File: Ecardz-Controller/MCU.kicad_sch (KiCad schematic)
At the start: 27 parts, among them J2 Conn_01x05, J5 Conn_01x04, U2 STM32G0C1RETx

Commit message: added eink and lcd pinouts
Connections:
- net LCD_PWM_BRIGHT: now reaches U2.28 (PB1)
- net SPI_LCD_DC: now reaches U2.29 (PB2)
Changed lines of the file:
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@@
+	(wire
+		(pts
+			(xy 137.16 93.98) (xy 161.29 93.98)
+		)
+		(stroke
+			(width 0)
+			(type default)
+		)
+	)
 	(wire
 		(pts
@@
 		(pts
 			(xy 85.09 50.8) (xy 69.85 50.8)
+		)
+		(stroke
+			(width 0)
+			(type default)
+		)
+	)
+	(wire
+		(pts
+			(xy 137.16 91.44) (xy 161.29 91.44)
 		)
 		(stroke
@@
 		)
 	)
+	(hierarchical_label "SPI_LCD_DC"
+		(shape input)
+		(at 161.29 93.98 0)
+		(fields_autoplaced yes)
+		(effects
+			(font
+				(size 1.27 1.27)
+			)
+			(justify left)
+		)
+	)
 	(hierarchical_label "USBC_UART_TX"
 		(shape input)
@@
 		(fields_autoplaced yes)
 		(effects
+			(font
+				(size 1.27 1.27)
+			)
+			(justify left)
+		)
+	)
+	(hierarchical_label "LCD_PWM_BRIGHT"
+		(shape input)
+		(at 161.29 91.44 0)
+		(fields_autoplaced yes)
+		(effects

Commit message: finished buzzer and button connections
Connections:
- net BUTTON6: now also U2.41 (PD9); no longer U2.37 (PA9/UCPD1_DBCC1)
- net BUZZER: now also U2.37 (PA9/UCPD1_DBCC1); no longer U2.41 (PD9)
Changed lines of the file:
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@@
-		)
-	)
-	(label "BUTTON6"
-		(at 139.7 68.58 0)
-		(fields_autoplaced yes)
-		(effects
-			(font
-				(size 1.27 1.27)
-			)
-			(justify left bottom)
 		)
 	)
@@
 		)
 	)
+	(label "BUTTON6"
+		(at 77.47 81.28 0)
+		(fields_autoplaced yes)
+		(effects
+			(font
+				(size 1.27 1.27)
+			)
+			(justify left bottom)
+		)
+	)
 	(label "SD_MISO"
 		(at 80.01 114.3 0)
@@
 		)
 	)
+	(hierarchical_label "BUTTONS"
+		(shape input)
+		(at 48.26 43.18 180)
+		(fields_autoplaced yes)
+		(effects
+			(font
+				(size 1.27 1.27)
+			)
+			(justify right)
+		)
+	)
+	(hierarchical_label "I2C_NFC_SCL"
+		(shape input)
+		(at 196.85 99.06 0)
+		(fields_autoplaced yes)
+		(effects
+			(font
+				(size 1.27 1.27)
+			)
+			(justify left)
+		)
+	)
+	(hierarchical_label "SPI_LCD_CS"
+		(shape input)
+		(at 161.29 88.9 0)
+		(fields_autoplaced yes)
+		(effects
+			(font
+				(size 1.27 1.27)
+			)
+			(justify left)
+		)
+	)
+	(hierarchical_label "SPI_EINK_SDA"
+		(shape input)
+		(at 74.93 88.9 180)
+		(fields_autoplaced yes)
+		(effects
+			(font
+				(size 1.27 1.27)
+			)
+			(justify right)
+		)
+	)
+	(hierarchical_label "SPI_EINK_CS"
+		(shape input)
+		(at 74.93 91.44 180)
+		(fields_autoplaced yes)
+		(effects
+			(font
+				(size 1.27 1.27)
+			)
+			(justify right)
+		)
+	)
+	(hierarchical_label "NFC_BUSY"
+		(shape input)
+		(at 196.85 101.6 0)
+		(fields_autoplaced yes)
+		(effects
+			(font
+				(size 1.27 1.27)
+			)
+			(justify left)
+		)
+	)
+	(hierarchical_label "SPI_LCD_MISO"
+		(shape input)
+		(at 161.29 60.96 0)
+		(fields_autoplaced yes)
+		(effects
+			(font
+				(size 1.27 1.27)
+			)
+			(justify left)
+		)
+	)
+	(hierarchical_label "NFC_I_SENSE"
+		(shape input)
+		(at 161.29 50.8 0)
+		(fields_autoplaced yes)
+		(effects
+			(font
+				(size 1.27 1.27)
+			)
+			(justify left)
+		)
+	)
+	(hierarchical_label "SPI_LCD_DC"
+		(shape input)
+		(at 161.29 93.98 0)
+		(fields_autoplaced yes)
+		(effects
+			(font
+				(size 1.27 1.27)
+			)
+			(justify left)
+		)
+	)
 	(hierarchical_label "BUZZER"
 		(shape input)
-		(at 74.93 81.28 180)
-		(fields_autoplaced yes)
-		(effects
-			(font
-				(size 1.27 1.27)
-			)
-			(justify right)
-		)
-	)
-	(hierarchical_label "BUTTONS"
-		(shape input)
-		(at 48.26 43.18 180)
-		(fields_autoplaced yes)
-		(effects
-			(font
-				(size 1.27 1.27)
-			)
-			(justify right)
-		)
-	)
-	(hierarchical_label "I2C_NFC_SCL"
-		(shape input)
-		(at 196.85 99.06 0)
-		(fields_autoplaced yes)
-		(effects
-			(font
-				(size 1.27 1.27)
-			)
-			(justify left)
-		)
-	)
-	(hierarchical_label "SPI_LCD_CS"
-		(shape input)
-		(at 161.29 88.9 0)
-		(fields_autoplaced yes)
-		(effects
-			(font
-				(size 1.27 1.27)
-			)
-			(justify left)
-		)
-	)
-	(hierarchical_label "SPI_EINK_SDA"
-		(shape input)
-		(at 74.93 88.9 180)
-		(fields_autoplaced yes)
-		(effects
-			(font
-				(size 1.27 1.27)
-			)
-			(justify right)
-		)
-	)
-	(hierarchical_label "SPI_EINK_CS"
-		(shape input)
-		(at 74.93 91.44 180)
-		(fields_autoplaced yes)
-		(effects
-			(font
-				(size 1.27 1.27)
-			)
-			(justify right)
-		)
-	)
-	(hierarchical_label "NFC_BUSY"
-		(shape input)
-		(at 196.85 101.6 0)
-		(fields_autoplaced yes)
-		(effects
-			(font
-				(size 1.27 1.27)
-			)
-			(justify left)
-		)
-	)
-	(hierarchical_label "SPI_LCD_MISO"
-		(shape input)
-		(at 161.29 60.96 0)
-		(fields_autoplaced yes)
-		(effects
-			(font
-				(size 1.27 1.27)
-			)
-			(justify left)
-		)
-	)
-	(hierarchical_label "NFC_I_SENSE"
-		(shape input)
-		(at 161.29 50.8 0)
-		(fields_autoplaced yes)
-		(effects
-			(font
-				(size 1.27 1.27)
-			)
-			(justify left)
-		)
-	)
-	(hierarchical_label "SPI_LCD_DC"
-		(shape input)
-		(at 161.29 93.98 0)
-		(fields_autoplaced yes)
-		(effects
+		(at 161.29 68.58 0)
+		(fields_autoplaced yes)
+		(effects

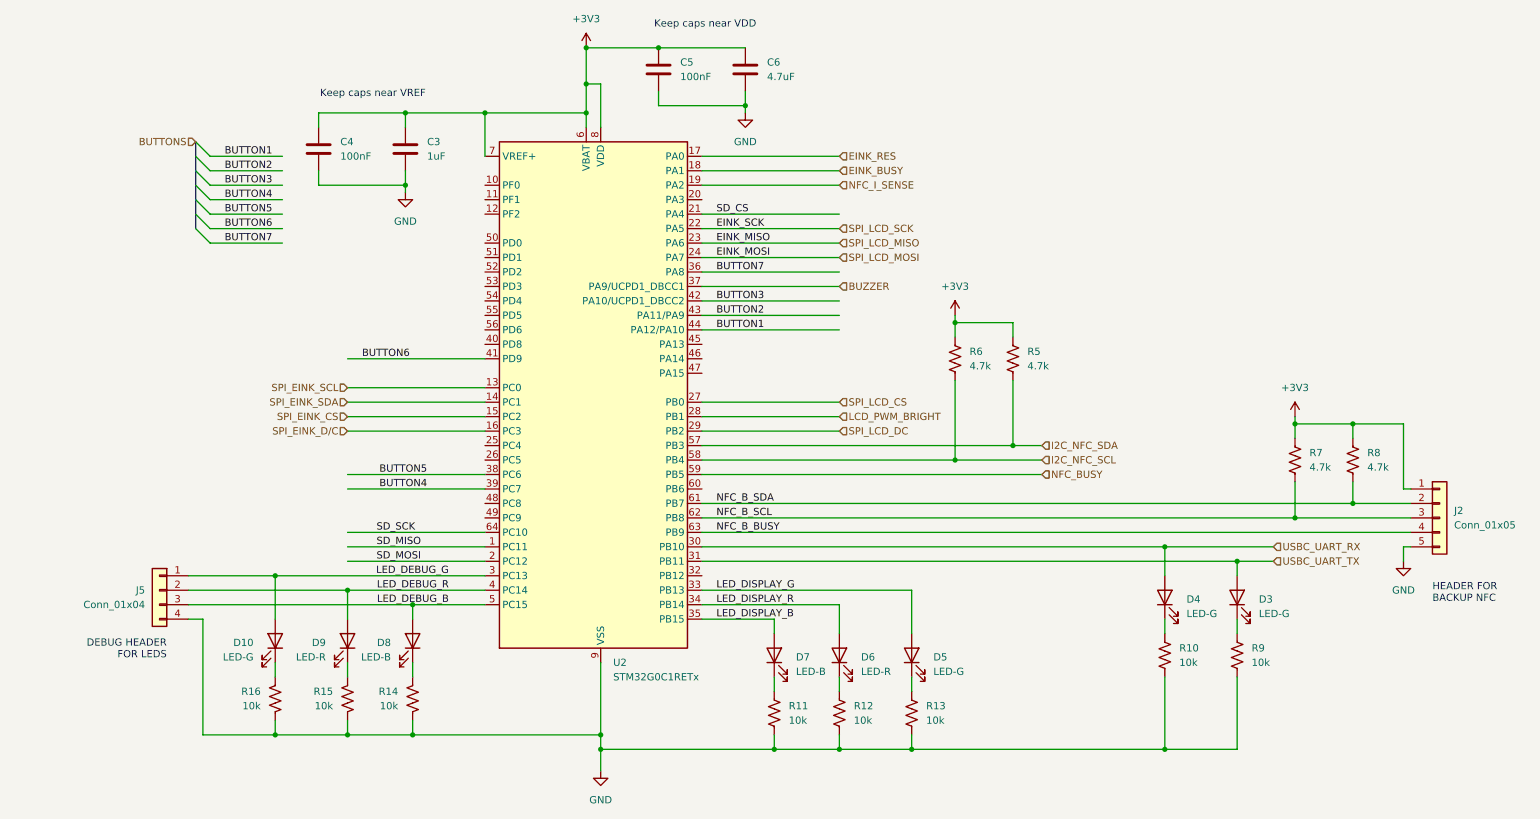
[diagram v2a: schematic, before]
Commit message: added LDO on buck output and SD card footprint
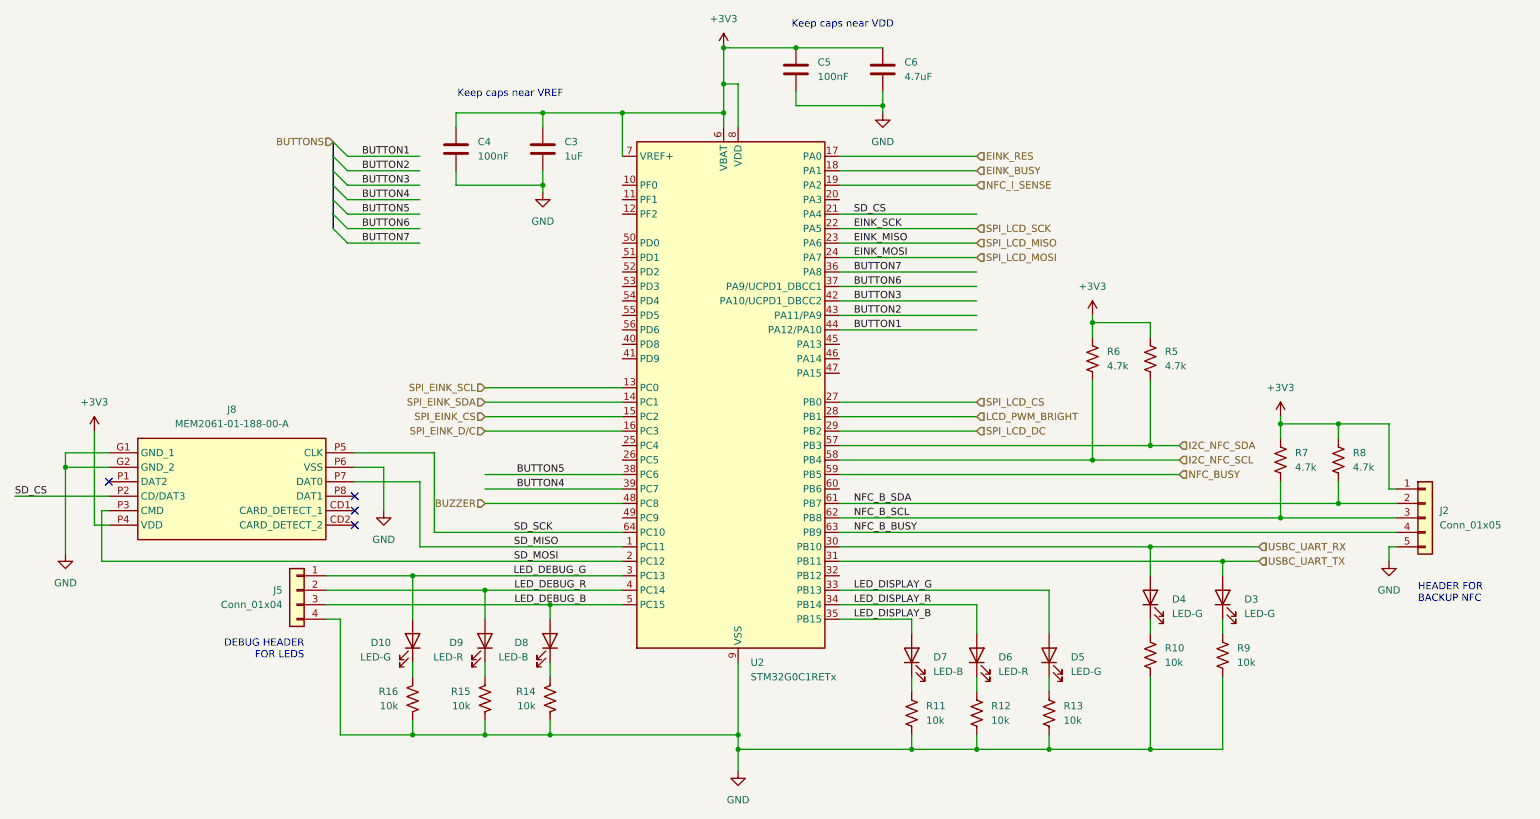
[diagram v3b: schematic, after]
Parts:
- added J8: MEM2061-01-188-00-A, MEM20610118800A, symbol SamacSys_Parts:MEM2061-01-188-00-A
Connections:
- net +3V3: now also J8.P4 (VDD)
- net BUTTON6: now also U2.37 (PA9/UCPD1_DBCC1); no longer U2.41 (PD9)
- net BUZZER: now also U2.48 (PC8); no longer U2.37 (PA9/UCPD1_DBCC1)
- net GND: now also J8.G1 (GND_1), J8.G2 (GND_2), J8.P6 (VSS)
- net SD_CS: now also J8.P2 (CD/DAT3)
- net SD_MISO: now also J8.P7 (DAT0)
- net SD_MOSI: now also J8.P3 (CMD)
- net SD_SCK: now also J8.P5 (CLK)
- no-connect marks 0 -> 4
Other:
- moved on the sheet: C3, C4, C5, C6, D10, D3, D4, D5, D6, D7, D8, D9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

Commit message: initial work on controller layout
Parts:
- renumbered C4 to C19, C3 to C20, C5 to C21, C6 to C22, D10 to D1, D9 to D2, D8 to D3, D7 to D4, D6 to D5, D5 to D6, D4 to D7, D3 to D8, J8 to J1, J5 to J2, J2 to J3, R12 to R10, R13 to R11, R6 to R12, R5 to R13, R10 to R14, R9 to R15, R7 to R16, R8 to R17, R16 to R6, R15 to R7, R14 to R8, R11 to R9, U2 to U1

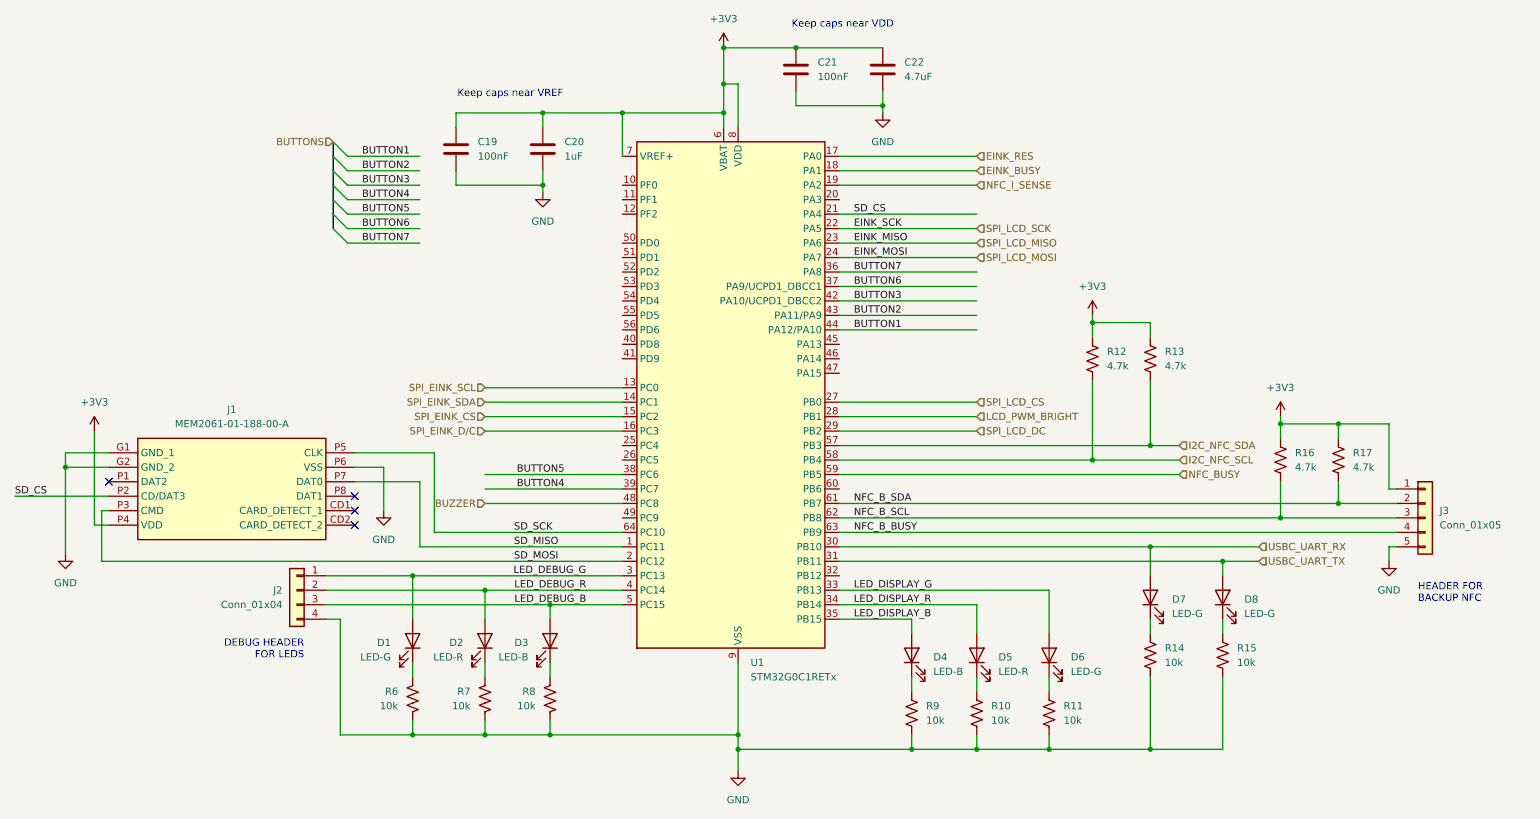
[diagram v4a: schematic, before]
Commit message: did bulk of controller layout apart from the antenna, added some NCs and other minor clean ups on schematic
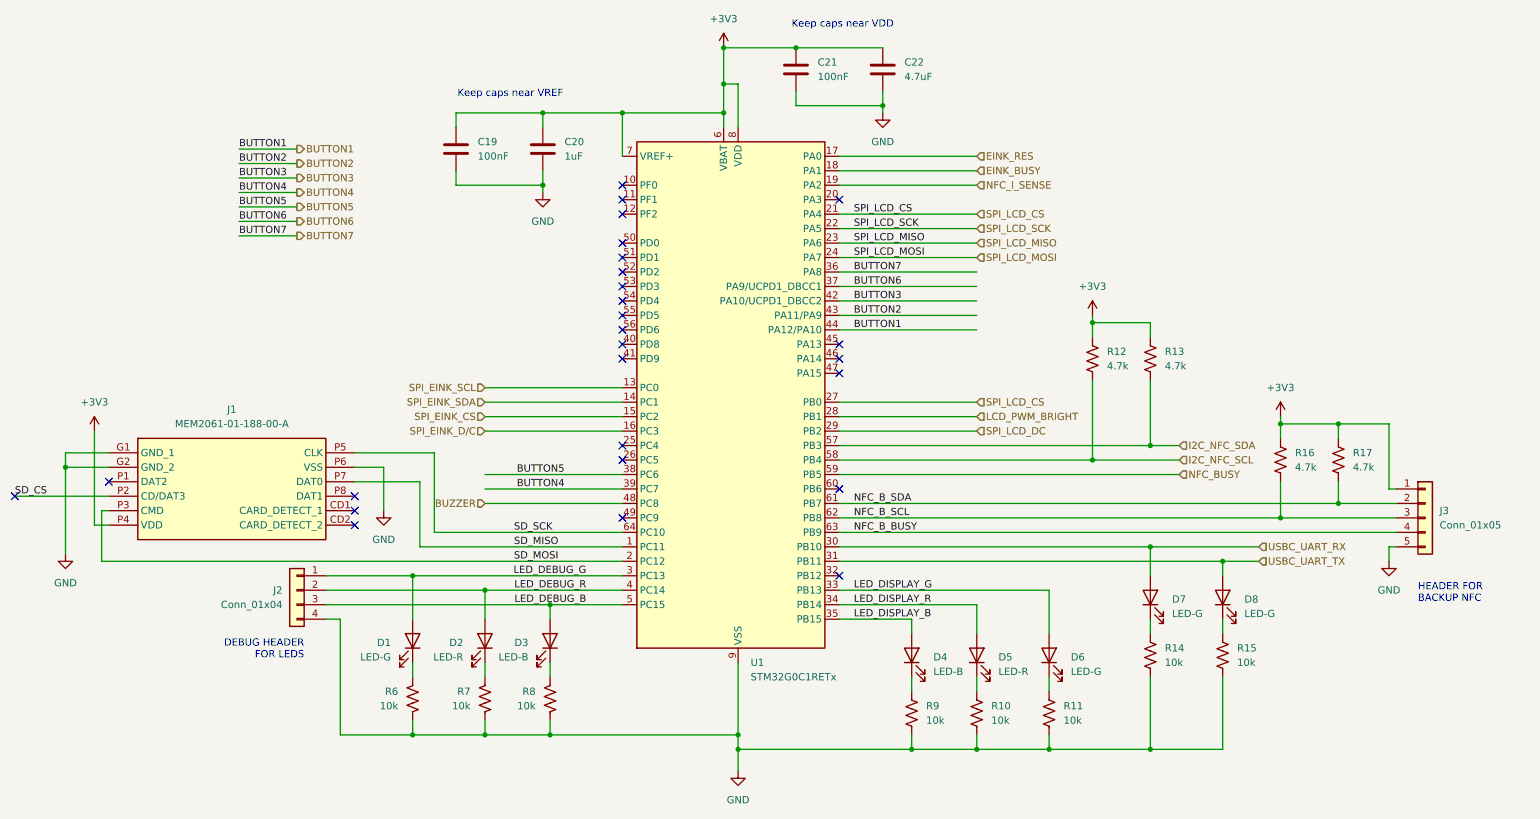
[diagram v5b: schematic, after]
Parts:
- J1: footprint MEM20610118800A -> samacsys:MEM20610118800A
- J2: footprint (none) -> Connector_PinHeader_2.54mm:PinHeader_1x04_P2.54mm_Vertical
- J3: footprint (none) -> Connector_PinHeader_2.54mm:PinHeader_1x05_P2.54mm_Vertical
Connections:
- net SD_CS: no longer U1.21 (PA4)
- net SPI_LCD_CS: now also U1.21 (PA4)
- no-connect marks 4 -> 26

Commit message: controller updates
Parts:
- removed D6: LED-G, LED_SMD:LED_0603_1608Metric_Pad1.05x0.95mm_HandSolder, symbol Device:LED
- removed R11: 10k, Resistor_SMD:R_0603_1608Metric_Pad0.98x0.95mm_HandSolder, symbol Device:R_US
- added TP11, TP12, TP13, TP14: TestPoint, TestPoint:TestPoint_Pad_D3.0mm, symbol Connector:TestPoint
- C19, C21: value 100nF -> 100n
- J1: Part Number (none) -> MEM2061-01-188-00-A
- J2: Part Number (none) -> 61300411121
- J3: Part Number (none) -> 61300511121
- renumbered R9 to R10, R10 to R11, R12 to R13, R13 to R14, R14 to R15, R15 to R16, R16 to R17, R17 to R18, R6 to R7, R7 to R8, R8 to R9
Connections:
- net EINK_BUSY: now also TP12.1
- net EINK_RES: now also TP13.1
- net LED_DEBUG_B: now also J2.1 (Pin_1), U1.3 (PC13); no longer J2.3 (Pin_3), U1.5 (PC15)
- net NFC_BUSY: now also TP11.1
- net NFC_B_BUSY: now also TP14.1
- net at D1.1 (K): now also R9.1; no longer R7.1
- net at D3.1 (K): now also R7.1; no longer R9.1
- removed net LED_DEBUG_G: D1.2 (A), J2.1 (Pin_1), U1.3 (PC13)
- net LED_DEBUG_R renamed LED_NFC_WORKING
- net LED_DISPLAY_G renamed PWR_INDICATOR
- new net LED_NFC_DONE: D1.2 (A), J2.3 (Pin_3), U1.5 (PC15)
